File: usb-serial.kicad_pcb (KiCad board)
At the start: 4 copper layers, 68.5 x 20.4 mm, 28 parts, among them J1 Conn_02x03_Odd_Even, U1 ACPL-M50L, U2 ACPL-M50L, U3 USBLC6-2SC6, U4 74LVC00, U6 Interface_USB_CP2102N-A01-GQF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

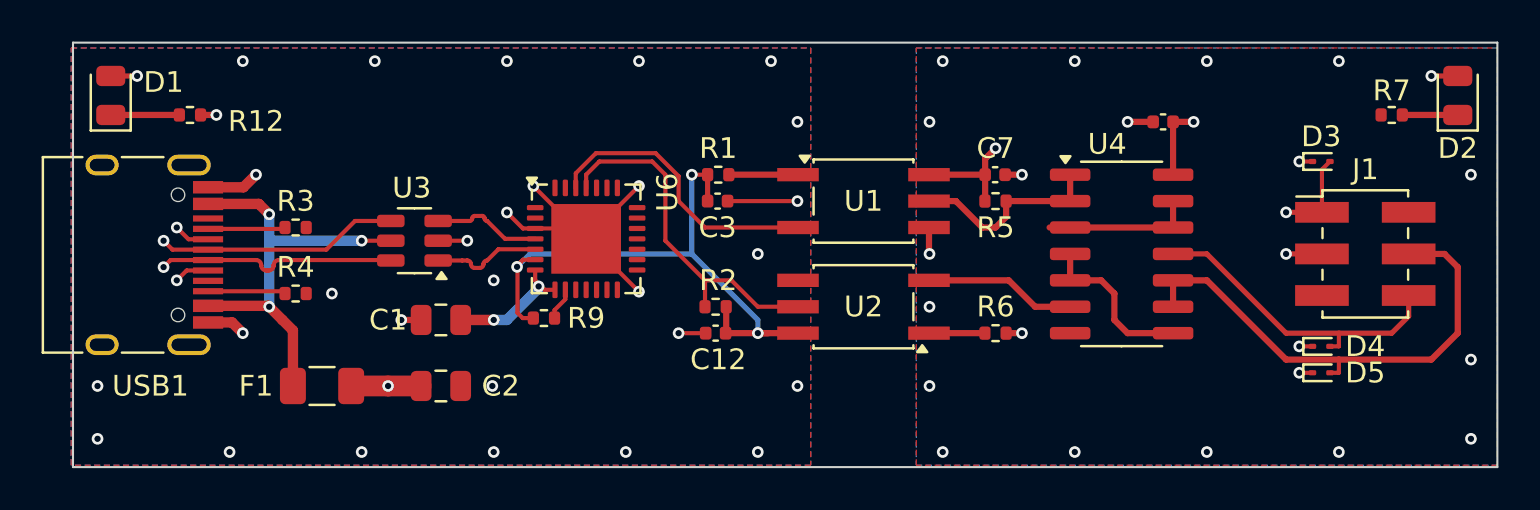
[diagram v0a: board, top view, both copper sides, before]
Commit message: Change to capacitive isolator
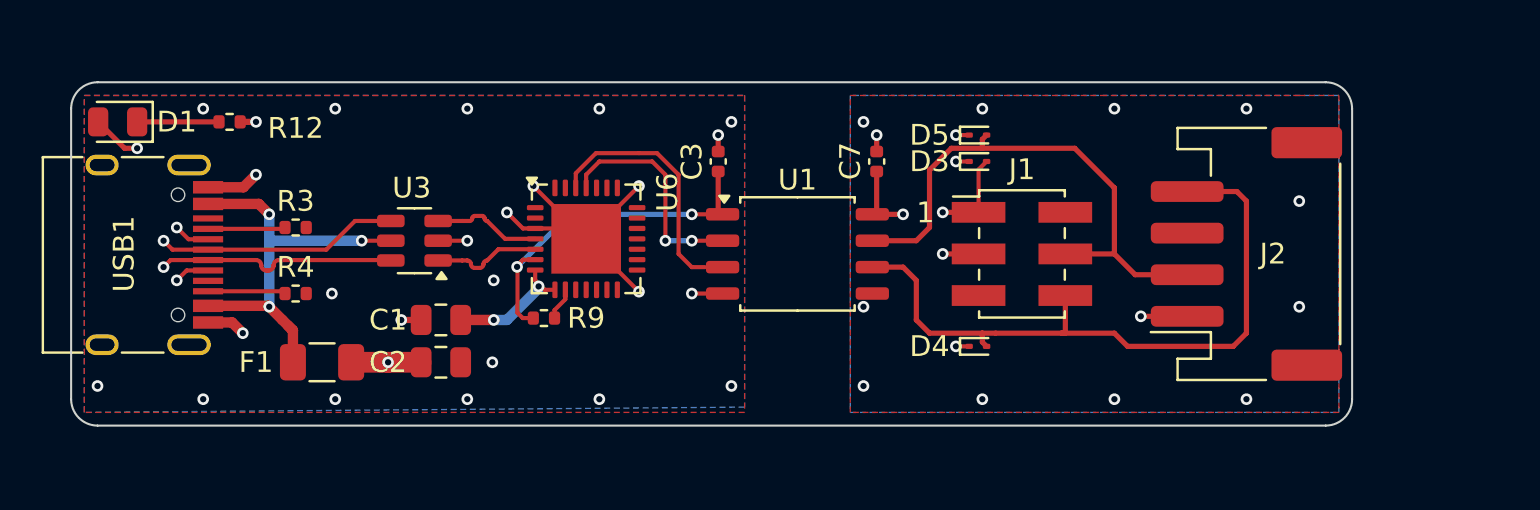
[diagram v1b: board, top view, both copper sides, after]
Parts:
- removed C12, C4: 100n, Capacitor_SMD:C_0402_1005Metric
- removed D2: LED, LED_SMD:LED_0805_2012Metric
- removed R1, R6: 1k, Resistor_SMD:R_0402_1005Metric
- removed R2, R5: 3k3, Resistor_SMD:R_0402_1005Metric
- removed R7: 330R, Resistor_SMD:R_0402_1005Metric
- removed U2: ACPL-M50L, Package_SO:SO-5_4.4x3.6mm_P1.27mm
- removed U4: 74LVC00, Package_SO:SOIC-14_3.9x8.7mm_P1.27mm
- added J2: Debug, Connector_JST:JST_PH_S4B-PH-SM4-TB_1x04-1MP_P2.00mm_Horizontal, F.Cu at (131.4, 54.0)
- added REF**: TUX, anders:TUX, B.Cu at (125.7, 54.0)
- J1: value Conn_02x03_Odd_Even -> Legacy debug
- U1: value ACPL-M50L -> MAX22246; footprint Package_SO:SO-5_4.4x3.6mm_P1.27mm -> Package_SO:SOP-8_5.28x5.23mm_P1.27mm
- moved D5 20.1 mm to (118.5, 48.3)
- moved D3 16.5 mm to (118.5, 49.5)
- moved D4 16.5 mm to (118.5, 58.4)
- moved J1 16.5 mm to (120.7, 54.0)
- moved C7 5.73 mm to (113.7, 49.5), turned to 90 degrees
- moved U1 4.07 mm to (109.9, 54.0)
- moved R12 1.93 mm to (82.5, 47.6)
- moved C3 1.91 mm to (106.0, 49.5), turned to 90 degrees
- moved D1 1.31 mm to (77.2, 47.6), turned to 180 degrees
- moved C2 1.14 mm to (92.7, 59.2)
- moved F1 1.14 mm to (87.0, 59.2)
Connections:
- net ~{TXD} renamed Net-(U1-IN2)
- C3 pad 1: VDD -> +3V3
- C7 pad 1: +3V3 -> VDD
- D3 pad 2: +3V3 -> VDD
- J1 pad 1: +3V3 -> VDD
- R9 pad 2: VDD -> +3V3
- U1 pad 1: Net-(U1-A1) -> +3V3
- U1 pad 4: GND1 -> GND
- U1 pad 5: ~{ISO_TXD} -> GND1
- U1 pad 6: +3V3 -> OUT_TxD
- U6 pad 25: ~{RXD} -> Net-(U1-OUT1)
- U6 pad 6: VDD -> +3V3
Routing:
- net VDD: track 29.3 -> 10.2 mm
- net OUT_TxD: track 15.3 -> 33.0 mm
- net ~{RXD}: track 17.1 -> 0.00 mm
- net Net-(U1-OUT1): track 0.00 -> 10.9 mm, vias 0 -> 2
- net ~{ISO_TXD}: track 9.55 -> 0.00 mm
- net Net-(U4-Pad4): track 8.02 -> 0.00 mm
- net ~{ISO_RXD}: track 7.60 -> 0.00 mm
- net Net-(U4-Pad12): track 7.21 -> 0.00 mm
- net Net-(U1-A1): track 3.32 -> 0.00 mm
- net IN_RxD: track 23.1 -> 26.1 mm
- net Net-(U2-A1): track 2.69 -> 0.00 mm
- net Net-(D2-K): track 2.66 -> 0.00 mm
- net GND1: track 6.95 -> 4.42 mm, vias 21 -> 16
- net GND: track 27.9 -> 25.5 mm, vias 29 -> 25
- net +3V3: track 15.3 -> 17.5 mm, vias 5 -> 2
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- added copper zone on In1.Cu, net VDD
- removed copper zone on In1.Cu, net +3V3
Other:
- board size 68.5 x 20.4 mm -> 61.6 x 16.5 mm
- board text added: "1"
- board text added: "LINUX"
- board text removed: "Isolated USB-Serial 3.3V TTL adapter By Anders Sandahl 2024"
